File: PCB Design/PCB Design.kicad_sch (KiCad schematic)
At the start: 20 parts, among them J1 Conn_01x02_Pin, J2 DX07S024WJ3R400, J4 Conn_02x16_Odd_Even, U1 INA219AxD, U2 IP2721, U4 AP22818AKEWT, U5 AP22818AKEWT

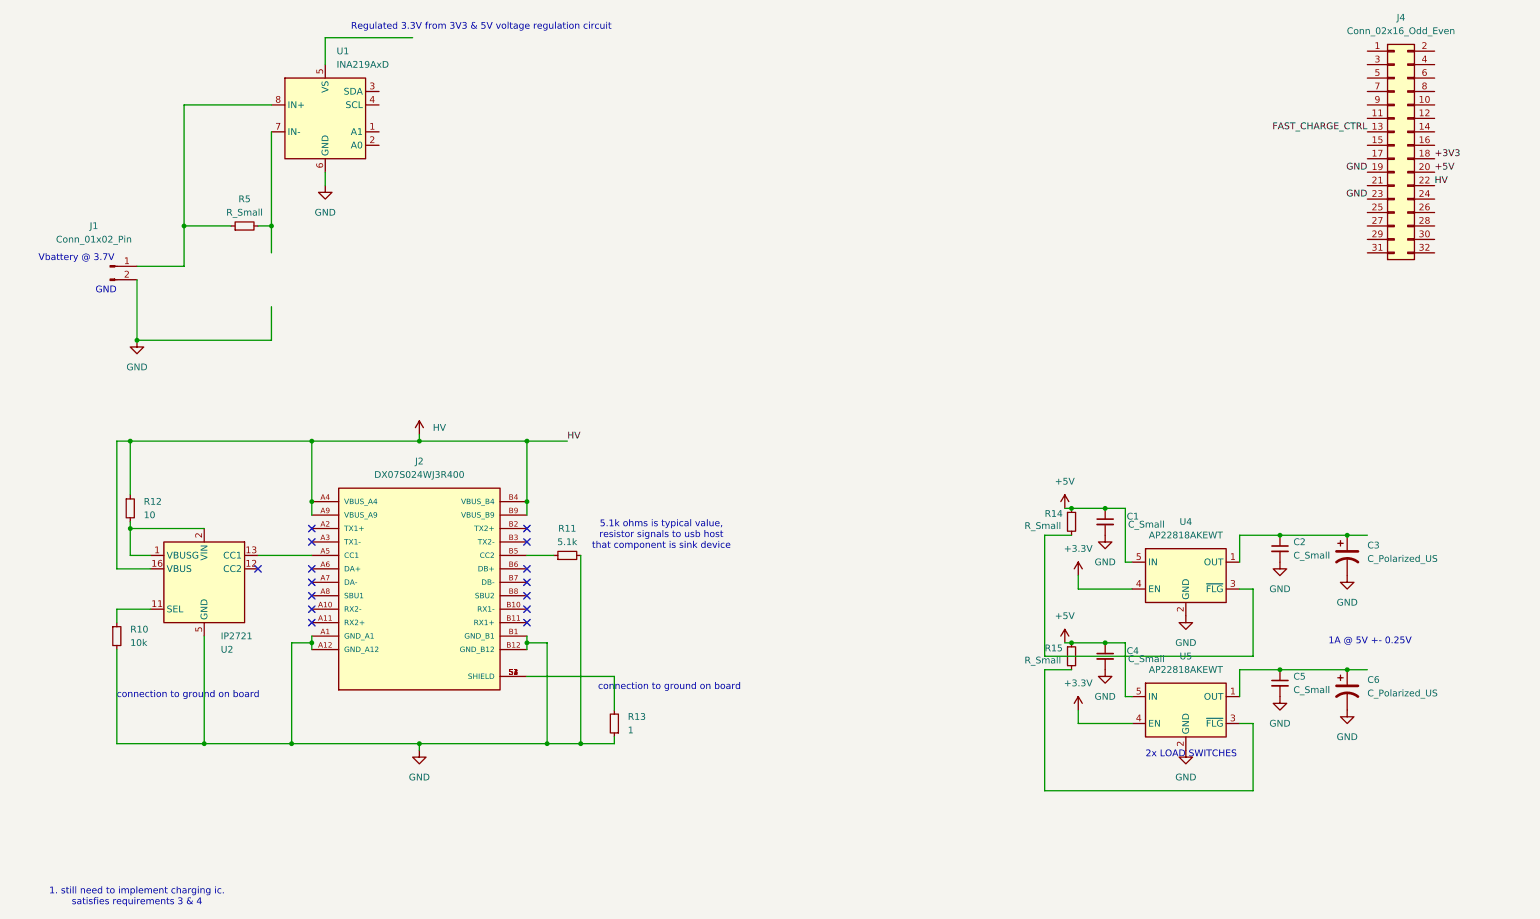
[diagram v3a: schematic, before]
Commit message: Added 2 H-Bridge ICs and configured the INA219 Battery monitor IC
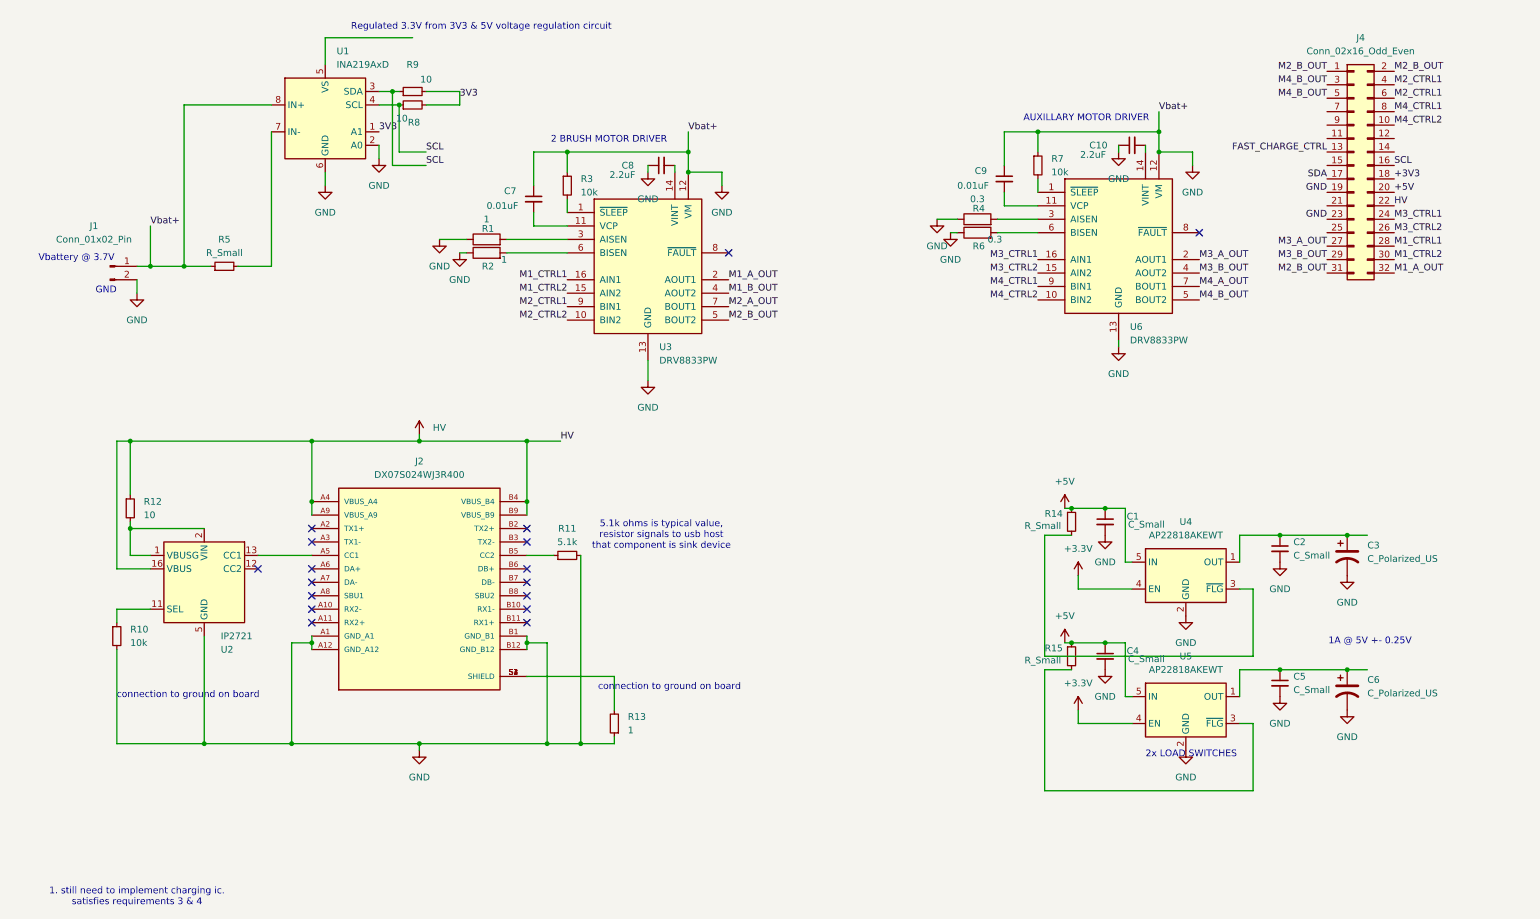
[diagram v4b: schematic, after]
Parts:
- added C10, C8: 2.2uF, symbol Device:C_Small
- added C7, C9: 0.01uF, symbol Device:C_Small
- added R1, R2: 1, symbol Device:R
- added R3, R7: 10k, symbol Device:R_Small
- added R4, R6: 0.3, symbol Device:R
- added R8, R9: 10, symbol Device:R_Small
- added U3, U6: DRV8833PW, Package_SO:TSSOP-16_4.4x5mm_P0.65mm, symbol Driver_Motor:DRV8833PW
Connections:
- net GND: now also J1.1 (Pin_1), R5.1, U1.2 (A0), U1.8 (IN+), C10.1, C7.1, C8.1, C9.1, R1.1, R2.1, R3.1, R4.1, R6.1, R7.1, U3.12 (VM), U3.13 (GND), U6.12 (VM), U6.13 (GND)
- net M2_B_OUT: now reaches J4.1 (Pin_1)
- net M2_B_OUT: now also J4.2 (Pin_2), J4.31 (Pin_31), U3.5 (BOUT2)
- net M4_CTRL2: now reaches J4.10 (Pin_10)
- net M4_CTRL2: now also U6.10 (BIN2)
- net SCL: now reaches J4.16 (Pin_16)
- net SCL: now also U1.3 (SDA), U1.4 (SCL), R8.1, R9.1
- net SDA: now reaches J4.17 (Pin_17)
- net M3_CTRL1: now reaches J4.24 (Pin_24)
- net M3_CTRL1: now also U6.16 (AIN1)
- net M3_CTRL2: now reaches J4.26 (Pin_26)
- net M3_CTRL2: now also U6.15 (AIN2)
- net M3_A_OUT: now reaches J4.27 (Pin_27)
- net M3_A_OUT: now also U6.2 (AOUT1)
- net M1_CTRL1: now reaches J4.28 (Pin_28)
- net M1_CTRL1: now also U3.16 (AIN1)
- net M3_B_OUT: now reaches J4.29 (Pin_29)
- net M3_B_OUT: now also U6.4 (AOUT2)
- net M4_B_OUT: now reaches J4.3 (Pin_3)
- net M4_B_OUT: now also J4.5 (Pin_5), U6.5 (BOUT2)
- net M1_CTRL2: now reaches J4.30 (Pin_30)
- net M1_CTRL2: now also U3.15 (AIN2)
- net M1_A_OUT: now reaches J4.32 (Pin_32)
- net M1_A_OUT: now also U3.2 (AOUT1)
- net M2_CTRL1: now reaches J4.4 (Pin_4)
- net M2_CTRL1: now also J4.6 (Pin_6), U3.9 (BIN1)
- net M4_CTRL1: now reaches J4.8 (Pin_8)
- net M4_CTRL1: now also U6.9 (BIN1)
- net 3V3: now reaches U1.1 (A1)
- net 3V3: now also R8.2, R9.2
- new net: R1.2, U3.3 (AISEN)
- new net: R2.2, U3.6 (BISEN)
- new net: R6.2, U6.6 (BISEN)
- new net: R4.2, U6.3 (AISEN)
- new net: R7.2, U6.1 (~{SLEEP})
- new net: C10.2, U6.14 (VINT)
- new net: C9.2, U6.11 (VCP)
- new net: R3.2, U3.1 (~{SLEEP})
- new net: C7.2, U3.11 (VCP)
- new net: C8.2, U3.14 (VINT)
- new net M1_B_OUT: U3.4 (AOUT2)
- new net M2_A_OUT: U3.7 (BOUT1)
- new net M2_CTRL2: U3.10 (BIN2)
- new net M4_A_OUT: U6.7 (BOUT1)
- no-connect marks 15 -> 17
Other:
- note added: "2 BRUSH MOTOR DRIVER"
- note added: "AUXILLARY MOTOR DRIVER"
- moved on the sheet: J4, R5
